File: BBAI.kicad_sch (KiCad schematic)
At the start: 2 parts, among them P1 BBAI - P8, P2 BBAI - P9

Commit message: I don't know
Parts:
- removed P2: BBAI - P9, symbol Scout_library:BBAIP9
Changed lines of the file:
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@@
 (kicad_sch (version 20230121) (generator eeschema)
   (paper "A4")
-  (symbol (lib_name "BBAIP9_1") (lib_id "Scout_library:BBAIP9") (at 106.045 85.725 0) (unit 1)
-    (in_bom yes) (on_board yes) (dnp no) (fields_autoplaced)
-    (property "Reference" "P2" (at 121.285 48.26 0)
-      (effects (font (size 1.27 1.27)))
-    )
-    (property "Value" "BBAI - P9" (at 121.285 50.8 0)
-      (effects (font (size 1.27 1.27)))
-    )
-    (property "Footprint" "" (at 106.045 85.725 0)
-      (effects (font (size 1.27 1.27)) hide)
-    )
-    (property "Datasheet" "~" (at 106.045 85.725 0)
-      (effects (font (size 1.27 1.27)) hide)
-    )
-    (pin "2")
-    (pin "25")
-    (pin "27")
-    (pin "29")
-    (pin "36")
-    (pin "37")
-    (pin "28")
-    (pin "13")
-    (pin "17")
-    (pin "38")
-    (pin "39")
-    (pin "4")
-    (pin "11")
-    (pin "21")
-    (pin "40")
-    (pin "10")
-    (pin "41")
-    (pin "42")
-    (pin "43")
-    (pin "44")
-    (pin "35")
-    (pin "45")
-    (pin "46")
-    (pin "33")
-    (pin "5")
-    (pin "6")
-    (pin "3")
-    (pin "32")
-    (pin "20")
-    (pin "1")
-    (pin "18")
-    (pin "15")
-    (pin "23")
-    (pin "22")
-    (pin "16")
-    (pin "24")
-    (pin "26")
-    (pin "30")
-    (pin "31")
-    (pin "12")
-    (pin "19")
-    (pin "14")
-    (pin "34")
-    (pin "8")
-    (pin "9")
-    (pin "E2")
-    (pin "E4")
-    (pin "7")
-    (pin "E1")
-    (pin "E3")
-    (instances
-      (project "Scout_Board"
-        (path "/e58a9779-147f-4c0c-a745-6e9bc8ec0357/f69c0108-1493-406f-9c14-edf38ee5c388"
-          (reference "P2") (unit 1)
-        )
-      )
-    )
-  )
   (symbol (lib_name "BBAIP8_1") (lib_id "Scout_library:BBAIP8") (at 60.96 88.265 0) (unit 1)
     (in_bom yes) (on_board yes) (dnp no) (fields_autoplaced)

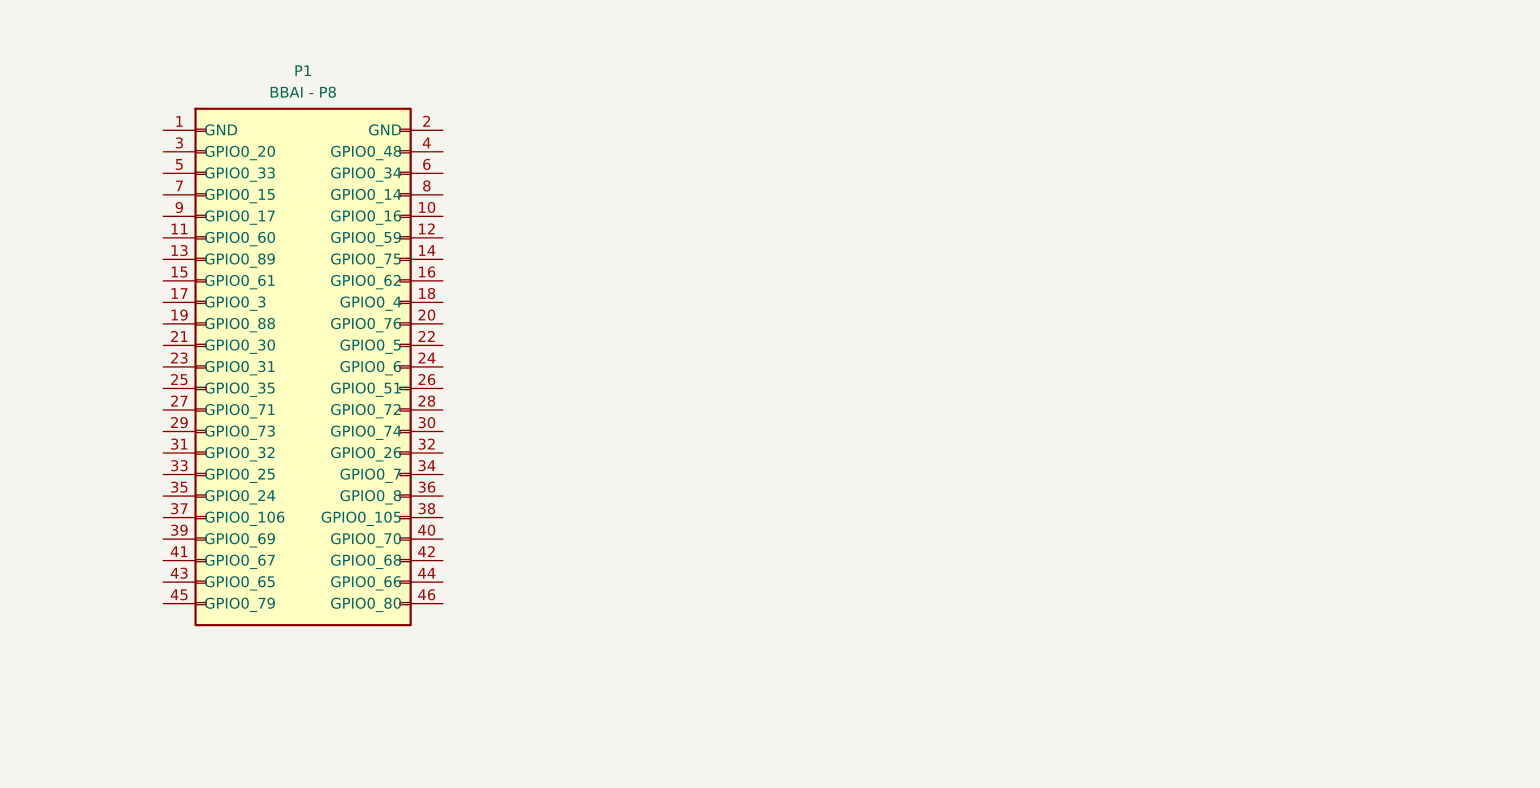
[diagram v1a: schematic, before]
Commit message: power board changes
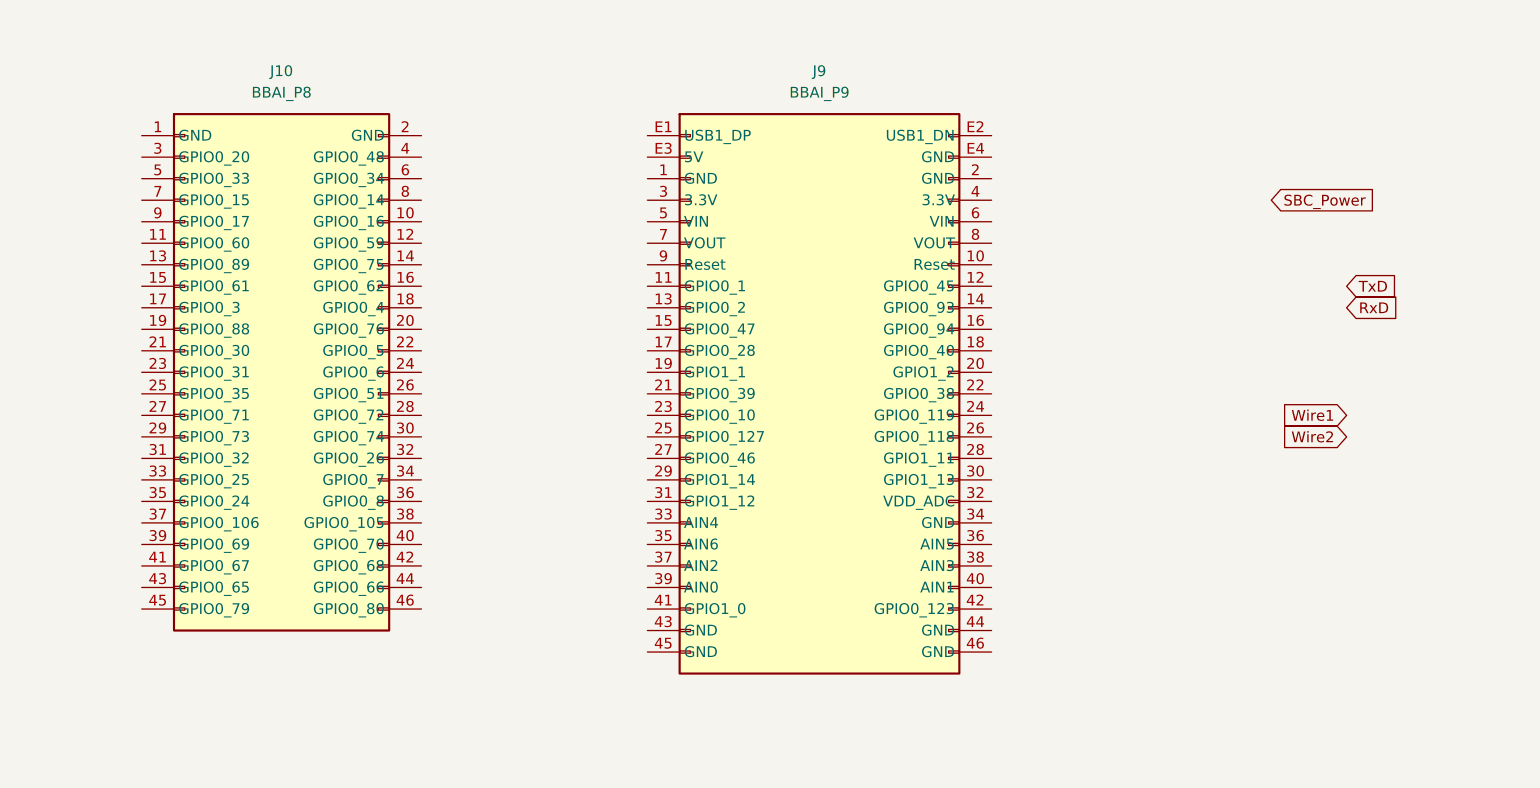
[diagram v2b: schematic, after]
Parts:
- removed P1: BBAI - P8, symbol Scout_library:BBAIP8
- added J10: BBAI_P8, Connector_PinSocket_2.54mm:PinSocket_2x23_P2.54mm_Vertical, symbol Custom Library:BBAI-64_P8
- added J9: BBAI_P9, Connector_PinSocket_2.54mm:PinSocket_2x25_P2.54mm_Vertical, symbol Custom Library:BBAI-64_P9

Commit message: New board test
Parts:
- renumbered J9 to J10, J10 to J11
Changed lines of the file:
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@@
+		)
+	)
+	(global_label "Sys_reset"
+		(shape input)
+		(at 186.69 62.23 0)
+		(fields_autoplaced yes)
+		(effects
+			(font
+				(size 1.27 1.27)
+			)
+			(justify left)
+		)
+		(property "Intersheetrefs" "${INTERSHEET_REFS}"
+			(at 198.5652 62.23 0)
+			(effects
+				(font
+					(size 1.27 1.27)
+				)
+				(justify left)
+				(hide yes)
+			)
 		)
 	)
@@
 		(dnp no)
 		(fields_autoplaced yes)
-		(property "Reference" "J9"
+		(property "Reference" "J10"
 			(at 133.35 53.34 0)
 			(effects
@@
 			(project ""
 				(path "/e58a9779-147f-4c0c-a745-6e9bc8ec0357/beec0241-a17d-4f9d-8cef-5e4a900fcdc6"
-					(reference "J9")
+					(reference "J10")
 					(unit 1)
 				)
@@
 		(dnp no)
 		(fields_autoplaced yes)
-		(property "Reference" "J10"
+		(property "Reference" "J11"
 			(at 69.85 53.34 0)
 			(effects
@@
 			(project ""
 				(path "/e58a9779-147f-4c0c-a745-6e9bc8ec0357/beec0241-a17d-4f9d-8cef-5e4a900fcdc6"
-					(reference "J10")
+					(reference "J11")
 					(unit 1)
 				)

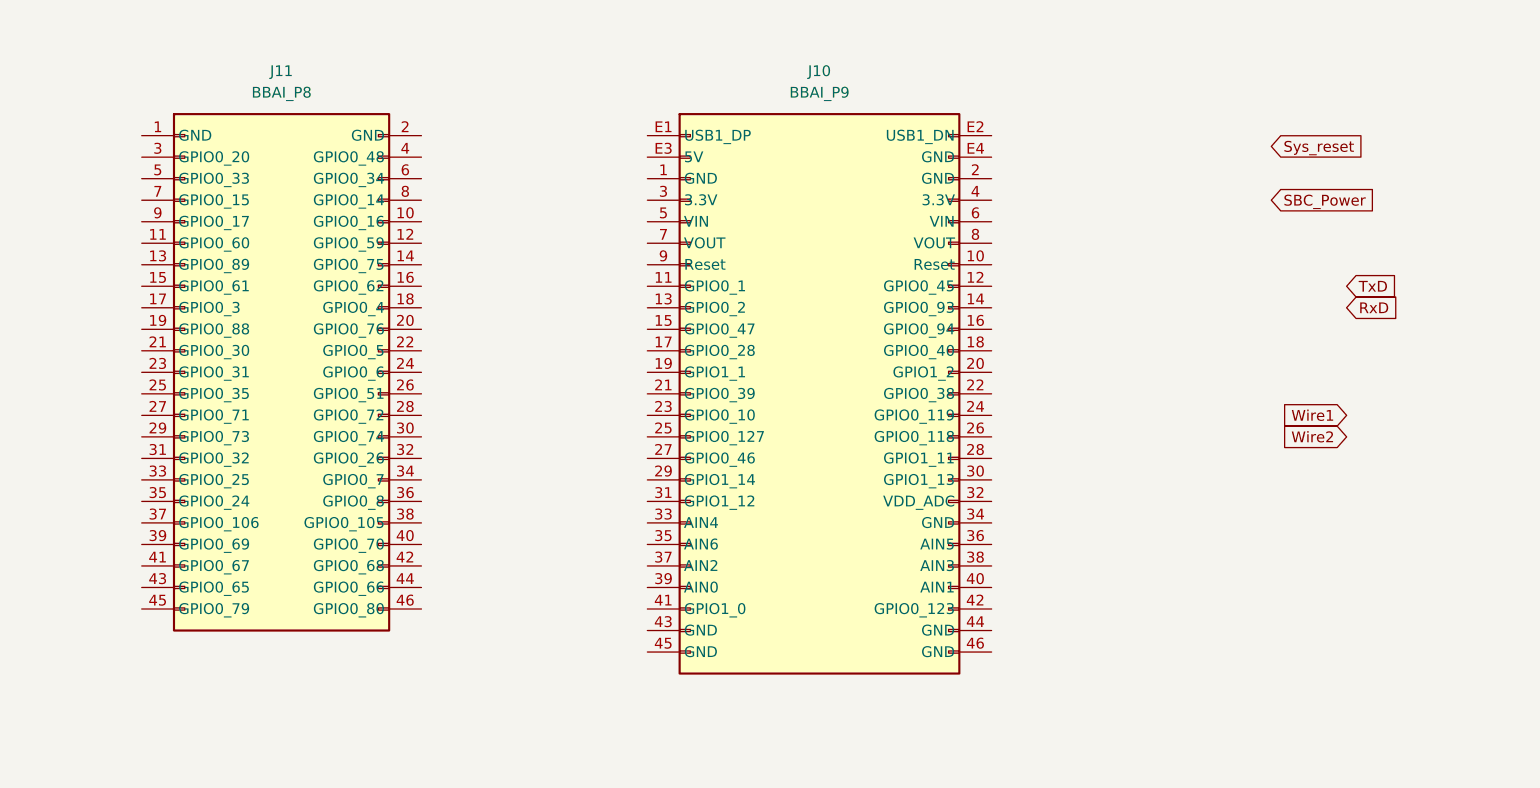
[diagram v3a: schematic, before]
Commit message: Layout updated with mounting holes
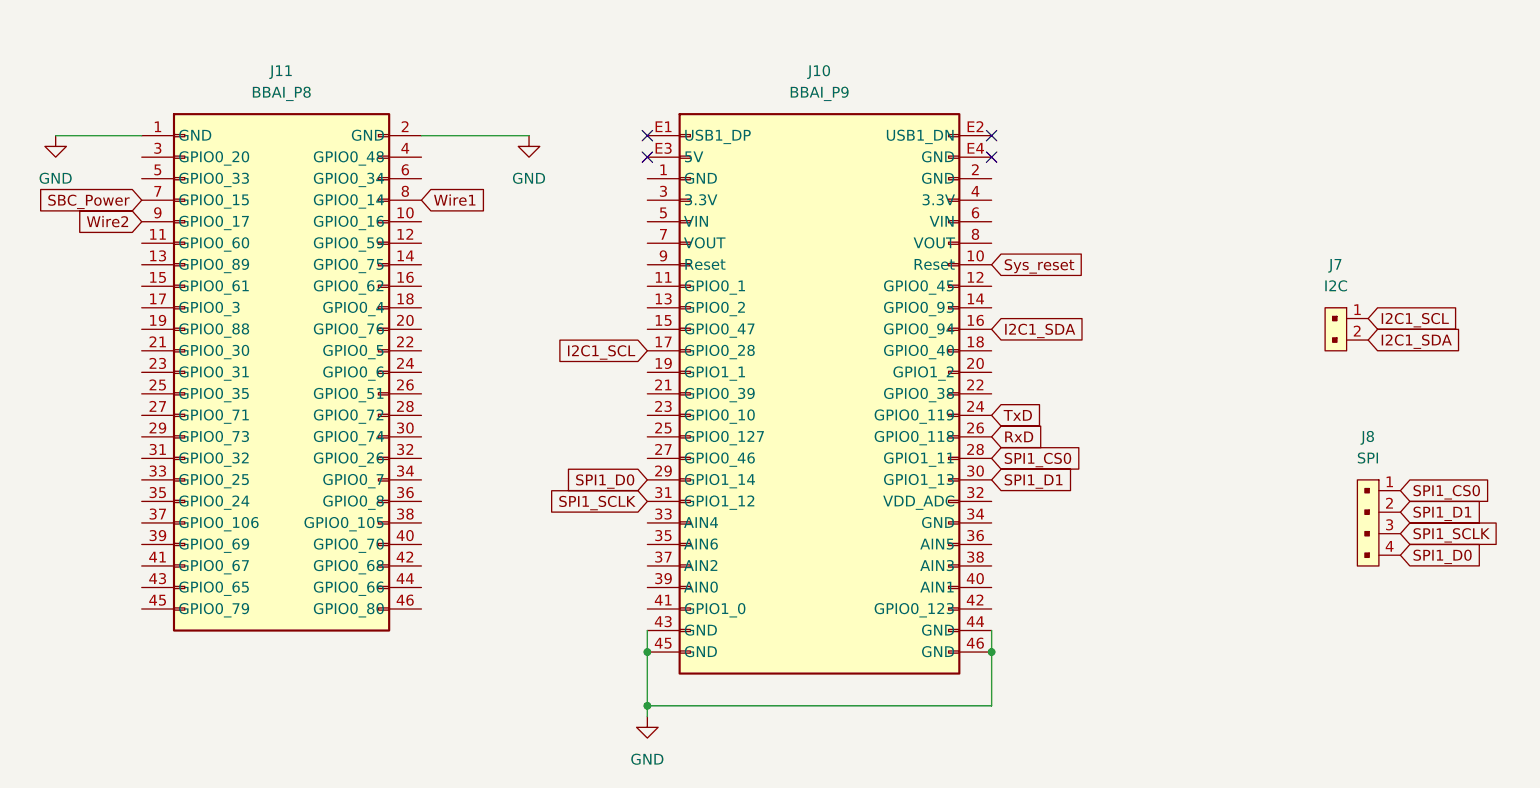
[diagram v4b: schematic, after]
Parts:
- added J7: I2C, digikey-footprints:PinHeader_1x2_P2.5mm_Drill1.1mm, symbol dk_Rectangular-Connectors-Headers-Male-Pins:B2B-XH-A_LF__SN_
- added J8: SPI, digikey-footprints:PinHeader_1x4_P2.5mm_Drill1.1mm, symbol dk_Rectangular-Connectors-Headers-Male-Pins:B4B-XH-A_LF__SN_
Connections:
- net RxD: now also J10.26 (GPIO0_118)
- net SBC_Power: now also J11.7 (GPIO0_15)
- net Sys_reset: now also J10.10 (Reset)
- net TxD: now also J10.24 (GPIO0_119)
- net Wire1: now also J11.8 (GPIO0_14)
- net Wire2: now also J11.9 (GPIO0_17)
- net I2C1_SDA: now reaches J10.16 (GPIO0_94)
- net I2C1_SDA: now also J7.2
- net I2C1_SCL: now reaches J10.17 (GPIO0_28)
- net I2C1_SCL: now also J7.1
- net SPI1_CS0: now reaches J10.28 (GPIO1_11)
- net SPI1_CS0: now also J8.1
- net SPI1_D0: now reaches J10.29 (GPIO1_14)
- net SPI1_D0: now also J8.4
- net SPI1_D1: now reaches J10.30 (GPIO1_13)
- net SPI1_D1: now also J8.2
- net SPI1_SCLK: now reaches J10.31 (GPIO1_12)
- net SPI1_SCLK: now also J8.3
- net GND: now reaches J10.43 (GND)
- net GND: now also J10.44 (GND), J10.45 (GND), J10.46 (GND), J11.1 (GND), J11.2 (GND)
- no-connect marks 0 -> 4

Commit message: Updated board
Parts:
- J10: footprint Connector_PinSocket_2.54mm:PinSocket_2x25_P2.54mm_Vertical -> Custom Library:BBAI-P9; LCSC (none) -> C7501604; Part Number (none) -> 0901310785
- J11: footprint Connector_PinSocket_2.54mm:PinSocket_2x23_P2.54mm_Vertical -> Custom Library:BBAI-P8; LCSC (none) -> C725895; Part Number (none) -> 0010897461
- J7: footprint digikey-footprints:PinHeader_1x2_P2.5mm_Drill1.1mm -> Connector_JST:JST_XH_B2B-XH-AM_1x02_P2.50mm_Vertical; LCSC (none) -> C158012; Part Number (none) -> B2B-XH-A-M
- J8: footprint digikey-footprints:PinHeader_1x4_P2.5mm_Drill1.1mm -> Connector_JST:JST_XH_B4B-XH-AM_1x04_P2.50mm_Vertical; LCSC (none) -> C161871; Part Number (none) -> B4B-XH-AM
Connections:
- net I2C1_SCL: now also J7.2; no longer J7.1
- net I2C1_SDA: now also J7.1; no longer J7.2
- net SPI1_CS0: now also J8.4; no longer J8.1
- net SPI1_D0: now also J8.3; no longer J8.4
- net SPI1_SCLK: now also J8.1; no longer J8.3
- no-connect marks 4 -> 12
